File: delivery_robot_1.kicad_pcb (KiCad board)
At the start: 4 copper layers, 100 x 100 mm, 106 parts, among them J1 SWD, J10 Port C/D breakout, J13 Pi 5 UART, J14 Pi 5 power, J15 Motor2 encoder, J16 MDD20A PWM2/DIR2/GND, J2 XT30PW-M, J4 BOOT0 jumper, J5 Power test points, J6 MDD20A PWM1/DIR1/GND, J7 Motor1 encoder, J8 Port A breakout, J9 Port B breakout, SW1 RESET, U1 STM32F091RCTx, U2 PTPSM63606RDLR, U3 TPS54202DDCR, U4 TPS7A8101DRBR, U5 PTPSM63606RDLR, U6 USBLC6-4SC6, U7 USBLC6-4SC6, Y3 8MHz

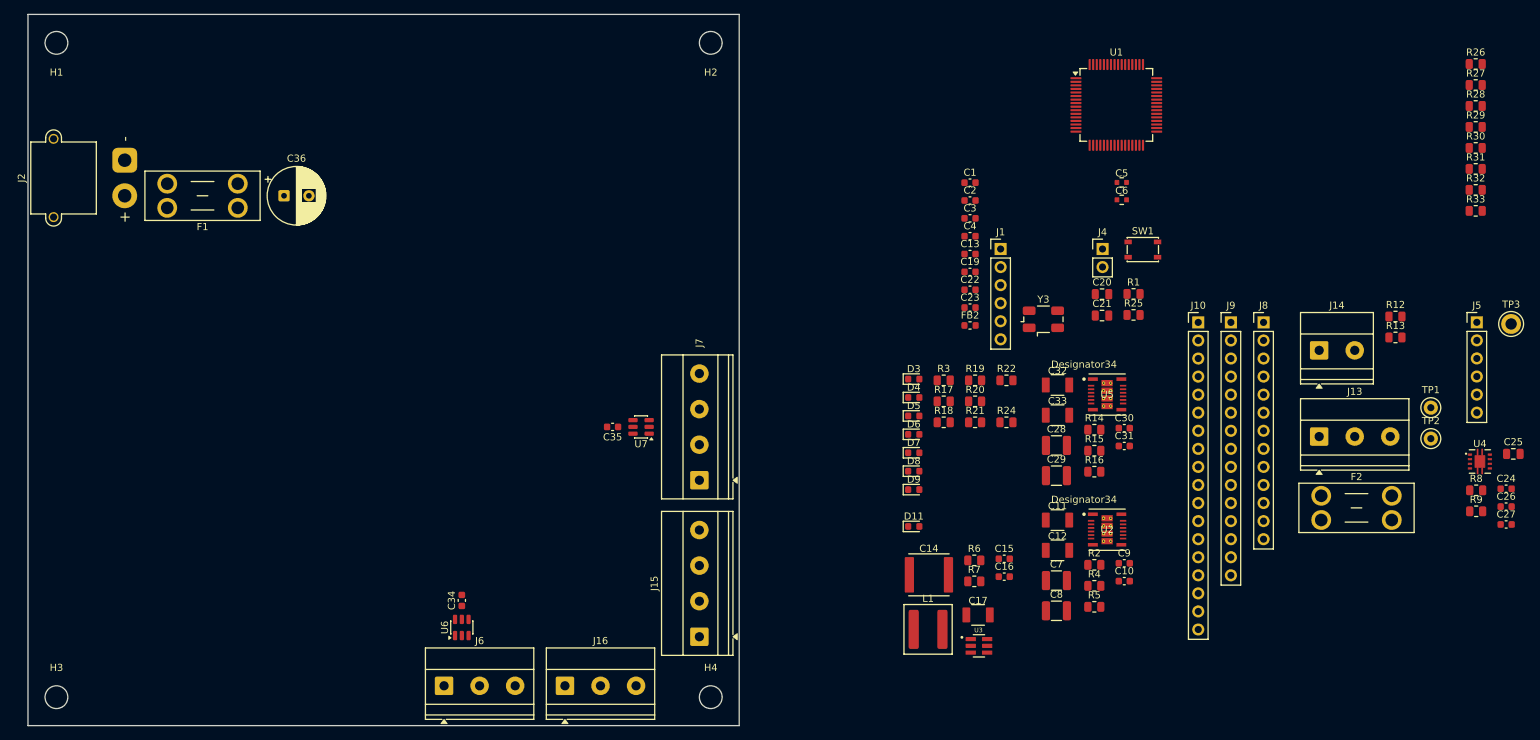
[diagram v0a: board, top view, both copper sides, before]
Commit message: Place buck converters, connectors and Pi power path on the PCB
Layout:
- Place the U2 (+5V_PI) 6 A buck group, and a copy of the same layout
  for the U5 (+5V_AUX) buck: U5, C28-C33, R14-R16.
- Place the U3 2 A buck (L1, R6/R7, C14-C17), the remaining J
  connectors (J1, J4, J5, J8-J10, J13, J14) and test point TP1.
- Add copper zones and vias. Set the default zone pad connection to
  solid.

Schematic:
- Remove F2 from the Pi 5 power path; +5V_PI now feeds J14 directly.
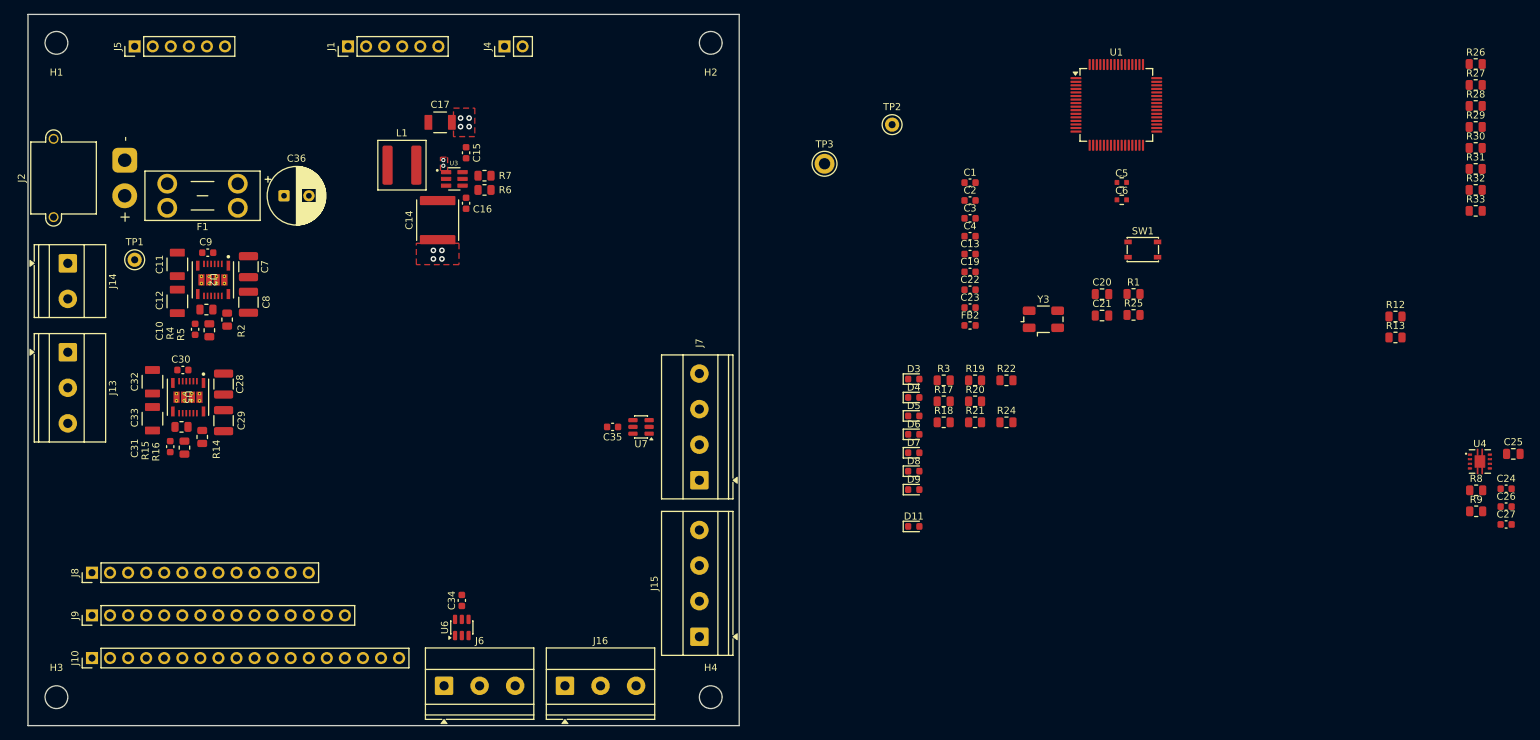
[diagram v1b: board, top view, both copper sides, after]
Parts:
- removed F2: 7.5A / 32VDC, Fuse:Fuseholder_Blade_Mini_Keystone_3568
- moved J5 192.7 mm to (100.0, 54.5), turned to 90 degrees
- moved TP1 183.4 mm to (100.0, 84.5)
- moved J14 176.4 mm to (90.6, 85.0), turned to -90 degrees
- moved J13 176.3 mm to (90.6, 97.5), turned to -90 degrees
- moved J8 168.4 mm to (94.0, 128.5), turned to 90 degrees
- moved J9 165.3 mm to (94.0, 134.5), turned to 90 degrees
- moved J10 162.5 mm to (94.0, 140.5), turned to 90 degrees
- moved C9 136.1 mm to (110.3, 83.5), turned to 180 degrees
- moved C10 135.4 mm to (108.5, 94.3), turned to 90 degrees
- moved C31 134.1 mm to (105.0, 110.8), turned to 90 degrees
- moved C30 132.6 mm to (106.8, 100.0), turned to 180 degrees
- moved R5 131.7 mm to (110.1, 91.5)
- moved U2 130.5 mm to (111.0, 87.3), turned to -90 degrees
- moved R4 129.5 mm to (110.5, 94.4), turned to 90 degrees
- moved U5 129.2 mm to (107.5, 103.8), turned to -90 degrees
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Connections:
- J14 pad 1: Net-(J14-Pin_1) -> +5V_PI
- TP2 pad 1: Net-(J14-Pin_1) -> +5V_PI
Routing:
- net GND: vias 0 -> 10
- added copper zone on F.Cu, net GND

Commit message: Place STM32, crystal and 3.3 V LDO; start routing crystal and GND
Layout:
- Place the STM32 (U1) with its decoupling capacitors, the Y3 crystal
  and its load capacitors, FB2 and R25.
- Place the 3.3 V LDO U4 (R8/R9, C24-C27) and lock it.
- Move the U3 5 V SYS buck group (L1, R6/R7, C14-C17) and lock it.
- Route OSC_IN/OSC_OUT and GND tracks, and add 18 GND vias.
- Remove isolated copper islands from zones.
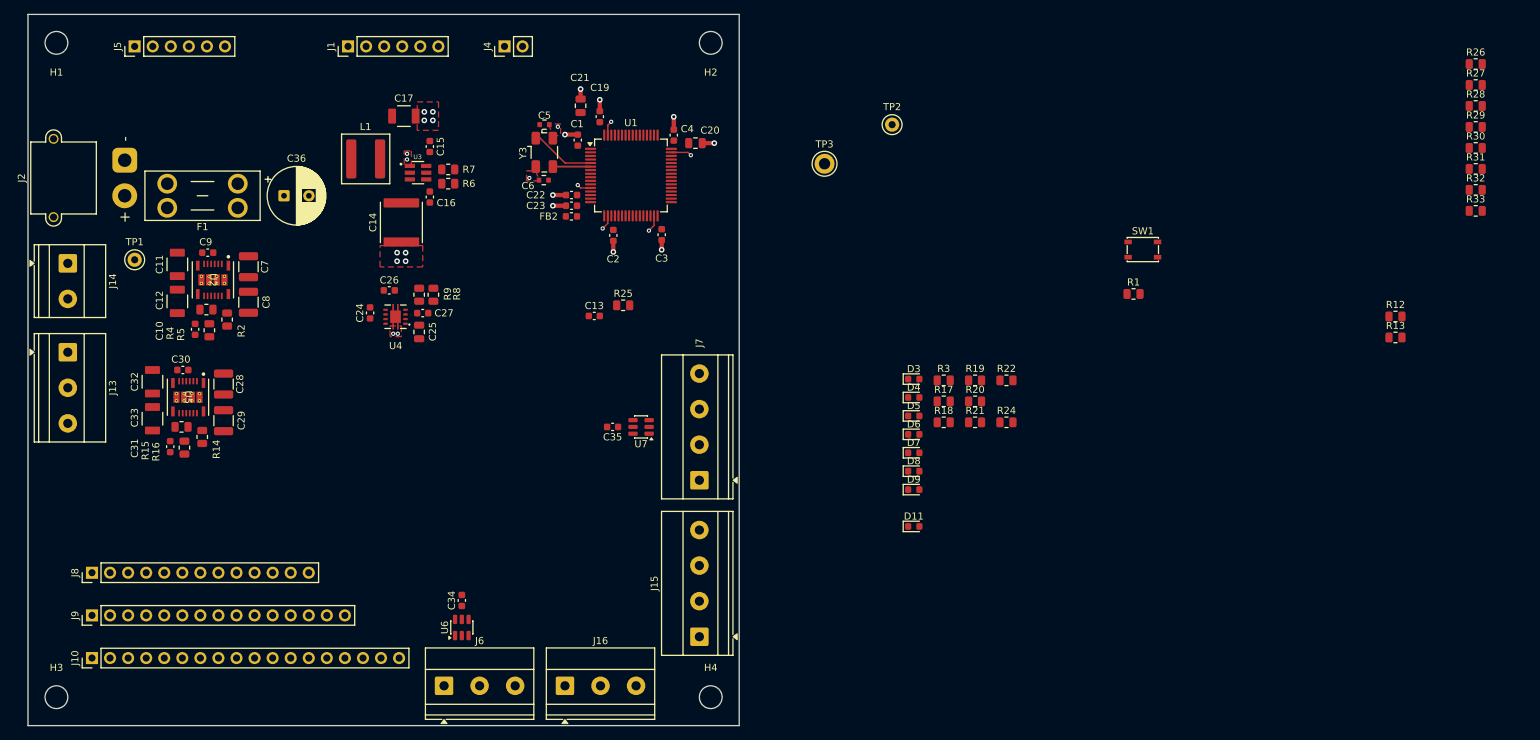
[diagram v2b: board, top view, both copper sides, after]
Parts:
- moved C24 161.6 mm to (133.1, 92.0), turned to 90 degrees
- moved C26 160.0 mm to (135.8, 88.8)
- moved C27 155.2 mm to (140.5, 92.0), turned to 180 degrees
- moved C25 154.8 mm to (140.0, 94.7), turned to -90 degrees
- moved U4 153.8 mm to (136.7, 92.5), turned to 180 degrees
- moved R9 151.7 mm to (140.0, 89.4), turned to 90 degrees
- moved R8 149.2 mm to (142.0, 89.4), turned to -90 degrees
- moved C5 81.6 mm to (157.6, 65.5)
- moved C6 81.3 mm to (157.5, 73.3), turned to 180 degrees
- moved C21 79.0 mm to (162.7, 62.9), turned to 90 degrees
- moved Y3 74.0 mm to (157.6, 69.4), turned to -90 degrees
- moved R25 71.8 mm to (168.7, 90.9)
- moved U1 69.0 mm to (169.8, 72.7)
- moved C20 61.0 mm to (178.8, 68.1)
- moved FB2 58.1 mm to (161.4, 78.4), turned to 180 degrees
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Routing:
- net GND: track 0.00 -> 26.3 mm, vias 10 -> 28
- net OSC_IN: track 0.00 -> 9.15 mm
- net OSC_OUT: track 0.00 -> 5.30 mm
